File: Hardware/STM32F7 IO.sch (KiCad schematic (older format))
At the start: 26 parts, among them U16 STM32F765ZGT6

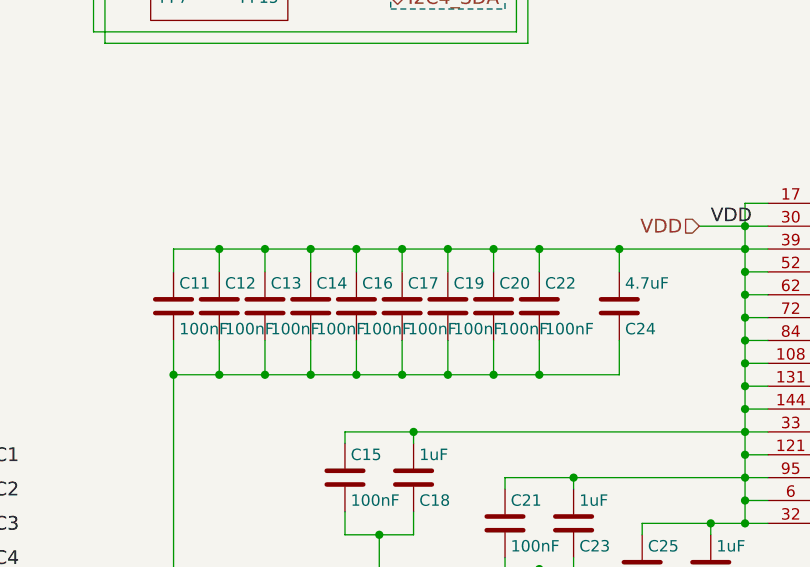
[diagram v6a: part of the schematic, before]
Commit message: Added ressistor footprint
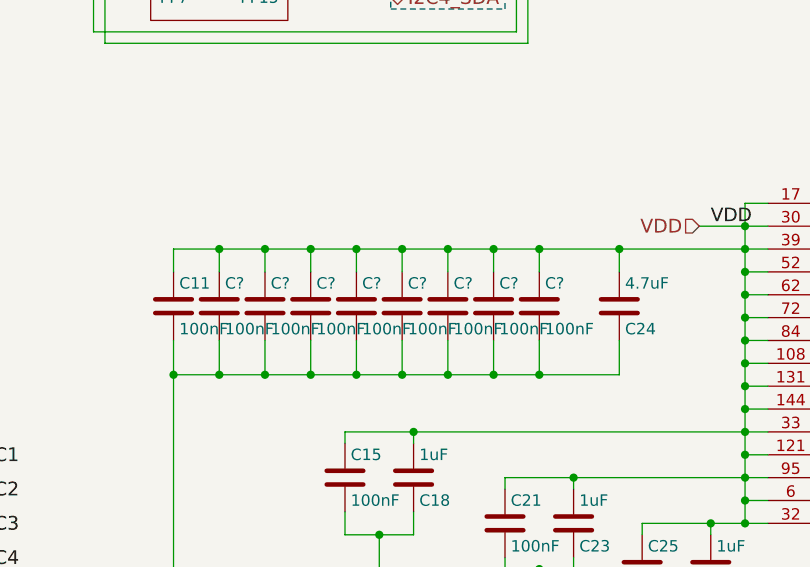
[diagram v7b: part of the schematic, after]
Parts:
- removed C12, C13, C14, C16, C17, C19, C20, C22: 100nF, symbol C
- added C? (x8): 100nF, Resistors_SMD:R_0603_HandSoldering, symbol C
- C11, C15, C18, C21, C23, C24, C25, C26, C27, C28, R54, R55, R56: footprint (none) -> Resistors_SMD:R_0603_HandSoldering
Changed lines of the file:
@@
 F 0 "C27" H 10375 5650 50  0000 L CNN
 F 1 "2.2uF" H 10375 5450 50  0000 L CNN
-F 2 "" H 10388 5400 50  0001 C CNN
+F 2 "Resistors_SMD:R_0603_HandSoldering" H 10388 5400 50  0001 C CNN
 F 3 "" H 10350 5550 50  0001 C CNN
 F 4 "CAPP-007" H 10350 5550 60  0001 C CNN "part_num"
@@
 F 0 "C28" H 10375 5950 50  0000 L CNN
 F 1 "2.2uF" H 10375 5750 50  0000 L CNN
-F 2 "" H 10388 5700 50  0001 C CNN
+F 2 "Resistors_SMD:R_0603_HandSoldering" H 10388 5700 50  0001 C CNN
 F 3 "" H 10350 5850 50  0001 C CNN
 F 4 "CAPP-007" H 10350 5850 60  0001 C CNN "part_num"
@@
 F 0 "C11" H 6375 5050 50  0000 L CNN
 F 1 "100nF" H 6375 4850 50  0000 L CNN
-F 2 "" H 6388 4800 50  0001 C CNN
+F 2 "Resistors_SMD:R_0603_HandSoldering" H 6388 4800 50  0001 C CNN
 F 3 "" H 6350 4950 50  0001 C CNN
 F 4 "CAPP-005" H 6350 4950 60  0001 C CNN "part_num"
@@
 F 0 "C24" H 8325 5050 50  0000 L CNN
 F 1 "4.7uF" H 8325 4850 50  0000 L CNN
-F 2 "" H 8338 4800 50  0001 C CNN
+F 2 "Resistors_SMD:R_0603_HandSoldering" H 8338 4800 50  0001 C CNN
 F 3 "" H 8300 4950 50  0001 C CNN
 F 4 "CAPP-006" H 8300 4950 60  0001 C CNN "part_num"
@@
 F 0 "C18" H 7425 5800 50  0000 L CNN
 F 1 "1uF" H 7425 5600 50  0000 L CNN
-F 2 "" H 7438 5550 50  0001 C CNN
+F 2 "Resistors_SMD:R_0603_HandSoldering" H 7438 5550 50  0001 C CNN
 F 3 "" H 7400 5700 50  0001 C CNN
 F 4 "CAPP-004" H 7400 5700 60  0001 C CNN "part_num"
@@
 F 0 "R54" V 8380 2300 50  0000 C CNN
 F 1 "100" V 8300 2300 50  0000 C CNN
-F 2 "" V 8230 2300 50  0001 C CNN
+F 2 "Resistors_SMD:R_0603_HandSoldering" V 8230 2300 50  0001 C CNN
 F 3 "" H 8300 2300 50  0001 C CNN
 F 4 "RESS-006" V 8300 2300 60  0001 C CNN "part_num"
@@
 F 0 "R55" V 8630 2300 50  0000 C CNN
 F 1 "100" V 8550 2300 50  0000 C CNN
-F 2 "" V 8480 2300 50  0001 C CNN
+F 2 "Resistors_SMD:R_0603_HandSoldering" V 8480 2300 50  0001 C CNN
 F 3 "" H 8550 2300 50  0001 C CNN
 F 4 "RESS-006" V 8550 2300 60  0001 C CNN "part_num"
@@
 F 0 "R56" V 8880 2300 50  0000 C CNN
 F 1 "100" V 8800 2300 50  0000 C CNN
-F 2 "" V 8730 2300 50  0001 C CNN
+F 2 "Resistors_SMD:R_0603_HandSoldering" V 8730 2300 50  0001 C CNN
 F 3 "" H 8800 2300 50  0001 C CNN
 F 4 "RESS-006" V 8800 2300 60  0001 C CNN "part_num"
@@
 F 0 "C23" H 8125 6000 50  0000 L CNN
 F 1 "1uF" H 8125 5800 50  0000 L CNN
-F 2 "" H 8138 5750 50  0001 C CNN
+F 2 "Resistors_SMD:R_0603_HandSoldering" H 8138 5750 50  0001 C CNN
 F 3 "" H 8100 5900 50  0001 C CNN
 F 4 "CAPP-004" H 8100 5900 60  0001 C CNN "part_num"
@@
 F 0 "C26" H 8725 6200 50  0000 L CNN
 F 1 "1uF" H 8725 6000 50  0000 L CNN
-F 2 "" H 8738 5950 50  0001 C CNN
+F 2 "Resistors_SMD:R_0603_HandSoldering" H 8738 5950 50  0001 C CNN
 F 3 "" H 8700 6100 50  0001 C CNN
 F 4 "CAPP-004" H 8700 6100 60  0001 C CNN "part_num"
 	1    8700 6100
 	1    0    0    1
-$EndComp
-$Comp
-L C C12
-U 1 1 595A3AD0
-P 6550 4950
-F 0 "C12" H 6575 5050 50  0000 L CNN
-F 1 "100nF" H 6575 4850 50  0000 L CNN
-F 2 "" H 6588 4800 50  0001 C CNN
-F 3 "" H 6550 4950 50  0001 C CNN
-F 4 "CAPP-005" H 6550 4950 60  0001 C CNN "part_num"
-	1    6550 4950
-	1    0    0    -1
-$EndComp
-$Comp
-L C C13
-U 1 1 595A3B1C
-P 6750 4950
-F 0 "C13" H 6775 5050 50  0000 L CNN
-F 1 "100nF" H 6775 4850 50  0000 L CNN
-F 2 "" H 6788 4800 50  0001 C CNN
-F 3 "" H 6750 4950 50  0001 C CNN
-F 4 "CAPP-005" H 6750 4950 60  0001 C CNN "part_num"
-	1    6750 4950
-	1    0    0    -1
-$EndComp
-$Comp
-L C C14
-U 1 1 595A3B74
-P 6950 4950
-F 0 "C14" H 6975 5050 50  0000 L CNN
-F 1 "100nF" H 6975 4850 50  0000 L CNN
-F 2 "" H 6988 4800 50  0001 C CNN
-F 3 "" H 6950 4950 50  0001 C CNN
-F 4 "CAPP-005" H 6950 4950 60  0001 C CNN "part_num"
-	1    6950 4950
-	1    0    0    -1
-$EndComp
-$Comp
-L C C16
-U 1 1 595A3BCA
-P 7150 4950
-F 0 "C16" H 7175 5050 50  0000 L CNN
-F 1 "100nF" H 7175 4850 50  0000 L CNN
-F 2 "" H 7188 4800 50  0001 C CNN
-F 3 "" H 7150 4950 50  0001 C CNN
-F 4 "CAPP-005" H 7150 4950 60  0001 C CNN "part_num"
-	1    7150 4950
-	1    0    0    -1
-$EndComp
-$Comp
-L C C17
-U 1 1 595A3C20
-P 7350 4950
-F 0 "C17" H 7375 5050 50  0000 L CNN
-F 1 "100nF" H 7375 4850 50  0000 L CNN
-F 2 "" H 7388 4800 50  0001 C CNN
-F 3 "" H 7350 4950 50  0001 C CNN
-F 4 "CAPP-005" H 7350 4950 60  0001 C CNN "part_num"
-	1    7350 4950
-	1    0    0    -1
-$EndComp
-$Comp
-L C C19
-U 1 1 595A3C76
-P 7550 4950
-F 0 "C19" H 7575 5050 50  0000 L CNN
-F 1 "100nF" H 7575 4850 50  0000 L CNN
-F 2 "" H 7588 4800 50  0001 C CNN
-F 3 "" H 7550 4950 50  0001 C CNN
-F 4 "CAPP-005" H 7550 4950 60  0001 C CNN "part_num"
-	1    7550 4950
-	1    0    0    -1
-$EndComp
-$Comp
-L C C20
-U 1 1 595A3CCA
-P 7750 4950
-F 0 "C20" H 7775 5050 50  0000 L CNN
-F 1 "100nF" H 7775 4850 50  0000 L CNN
-F 2 "" H 7788 4800 50  0001 C CNN
-F 3 "" H 7750 4950 50  0001 C CNN
-F 4 "CAPP-005" H 7750 4950 60  0001 C CNN "part_num"
-	1    7750 4950
-	1    0    0    -1
-$EndComp
-$Comp
-L C C22
-U 1 1 595A3D20
-P 7950 4950
-F 0 "C22" H 7975 5050 50  0000 L CNN
-F 1 "100nF" H 7975 4850 50  0000 L CNN
-F 2 "" H 7988 4800 50  0001 C CNN
-F 3 "" H 7950 4950 50  0001 C CNN
-F 4 "CAPP-005" H 7950 4950 60  0001 C CNN "part_num"
-	1    7950 4950
-	1    0    0    -1
 $EndComp
 $Comp
@@
 F 0 "C25" H 8425 6200 50  0000 L CNN
 F 1 "100nF" H 8425 6000 50  0000 L CNN
-F 2 "" H 8438 5950 50  0001 C CNN
+F 2 "Resistors_SMD:R_0603_HandSoldering" H 8438 5950 50  0001 C CNN
 F 3 "" H 8400 6100 50  0001 C CNN
 F 4 "CAPP-005" H 8400 6100 60  0001 C CNN "part_num"
@@
 F 0 "C21" H 7825 6000 50  0000 L CNN
 F 1 "100nF" H 7825 5800 50  0000 L CNN
-F 2 "" H 7838 5750 50  0001 C CNN
+F 2 "Resistors_SMD:R_0603_HandSoldering" H 7838 5750 50  0001 C CNN
 F 3 "" H 7800 5900 50  0001 C CNN
 F 4 "CAPP-005" H 7800 5900 60  0001 C CNN "part_num"
@@
 F 0 "C15" H 7125 5800 50  0000 L CNN
 F 1 "100nF" H 7125 5600 50  0000 L CNN
-F 2 "" H 7138 5550 50  0001 C CNN
+F 2 "Resistors_SMD:R_0603_HandSoldering" H 7138 5550 50  0001 C CNN
 F 3 "" H 7100 5700 50  0001 C CNN
 F 4 "CAPP-005" H 7100 5700 60  0001 C CNN "part_num"
@@
 	1    0    0    -1
 $EndComp
+$Comp
+L C C?
+U 1 1 595B66E8
+P 6550 4950
+F 0 "C?" H 6575 5050 50  0000 L CNN
+F 1 "100nF" H 6575 4850 50  0000 L CNN
+F 2 "Resistors_SMD:R_0603_HandSoldering" H 6588 4800 50  0001 C CNN
+F 3 "" H 6550 4950 50  0001 C CNN
+F 4 "CAPP-005" H 6550 4950 60  0001 C CNN "part_num"
+	1    6550 4950
+	1    0    0    -1
+$EndComp
+$Comp
+L C C?
+U 1 1 595B6734
+P 6750 4950
+F 0 "C?" H 6775 5050 50  0000 L CNN
+F 1 "100nF" H 6775 4850 50  0000 L CNN
+F 2 "Resistors_SMD:R_0603_HandSoldering" H 6788 4800 50  0001 C CNN
+F 3 "" H 6750 4950 50  0001 C CNN
+F 4 "CAPP-005" H 6750 4950 60  0001 C CNN "part_num"
+	1    6750 4950
+	1    0    0    -1
+$EndComp
+$Comp
+L C C?
+U 1 1 595B6780
+P 6950 4950
+F 0 "C?" H 6975 5050 50  0000 L CNN
+F 1 "100nF" H 6975 4850 50  0000 L CNN
+F 2 "Resistors_SMD:R_0603_HandSoldering" H 6988 4800 50  0001 C CNN
+F 3 "" H 6950 4950 50  0001 C CNN
+F 4 "CAPP-005" H 6950 4950 60  0001 C CNN "part_num"
+	1    6950 4950
+	1    0    0    -1
+$EndComp
+$Comp
+L C C?
+U 1 1 595B67CE
+P 7150 4950
+F 0 "C?" H 7175 5050 50  0000 L CNN
+F 1 "100nF" H 7175 4850 50  0000 L CNN
+F 2 "Resistors_SMD:R_0603_HandSoldering" H 7188 4800 50  0001 C CNN
+F 3 "" H 7150 4950 50  0001 C CNN
+F 4 "CAPP-005" H 7150 4950 60  0001 C CNN "part_num"
+	1    7150 4950
+	1    0    0    -1
+$EndComp
+$Comp
+L C C?
+U 1 1 595B681E
+P 7350 4950
+F 0 "C?" H 7375 5050 50  0000 L CNN
+F 1 "100nF" H 7375 4850 50  0000 L CNN
+F 2 "Resistors_SMD:R_0603_HandSoldering" H 7388 4800 50  0001 C CNN
+F 3 "" H 7350 4950 50  0001 C CNN
+F 4 "CAPP-005" H 7350 4950 60  0001 C CNN "part_num"
+	1    7350 4950
+	1    0    0    -1
+$EndComp
+$Comp
+L C C?
+U 1 1 595B6870
+P 7550 4950
+F 0 "C?" H 7575 5050 50  0000 L CNN
+F 1 "100nF" H 7575 4850 50  0000 L CNN
+F 2 "Resistors_SMD:R_0603_HandSoldering" H 7588 4800 50  0001 C CNN
+F 3 "" H 7550 4950 50  0001 C CNN
+F 4 "CAPP-005" H 7550 4950 60  0001 C CNN "part_num"
+	1    7550 4950
+	1    0    0    -1
+$EndComp
+$Comp
+L C C?
+U 1 1 595B68C4
+P 7750 4950
+F 0 "C?" H 7775 5050 50  0000 L CNN
+F 1 "100nF" H 7775 4850 50  0000 L CNN
+F 2 "Resistors_SMD:R_0603_HandSoldering" H 7788 4800 50  0001 C CNN
+F 3 "" H 7750 4950 50  0001 C CNN
+F 4 "CAPP-005" H 7750 4950 60  0001 C CNN "part_num"
+	1    7750 4950
+	1    0    0    -1
+$EndComp
+$Comp
+L C C?
+U 1 1 595B691A
+P 7950 4950
+F 0 "C?" H 7975 5050 50  0000 L CNN
+F 1 "100nF" H 7975 4850 50  0000 L CNN
+F 2 "Resistors_SMD:R_0603_HandSoldering" H 7988 4800 50  0001 C CNN
+F 3 "" H 7950 4950 50  0001 C CNN
+F 4 "CAPP-005" H 7950 4950 60  0001 C CNN "part_num"
+	1    7950 4950
+	1    0    0    -1
+$EndComp

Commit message: PCB?!
Added initial PCB file with ratsnest. footprint library still needs to
be setup.
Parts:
- removed SH25: SHORT, symbol SHORT
- added R81: 0, Resistors_SMD:R_0603_HandSoldering, symbol R
- D17, D18, D19: footprint (none) -> LEDs:LED_0603
- U16: footprint (none) -> Housings_QFP:LQFP-144_20x20mm_Pitch0.5mm
- gave numbers to parts that had none: 8
- renumbered R54 to R78, R55 to R79, R56 to R80
